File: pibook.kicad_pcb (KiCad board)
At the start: 2 copper layers, 85 x 85 mm, 161 parts, among them IC1 ATTINY48-A, J1 ComputeModule, J2 TRS_JACK_3PIN, P1 CONN_01X40, P2 USB_OTG, P3 CONN_01X02, P4 CONN_02X05, P5 USB_A, P6 CONN_02X06, P7 CONN_01X20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

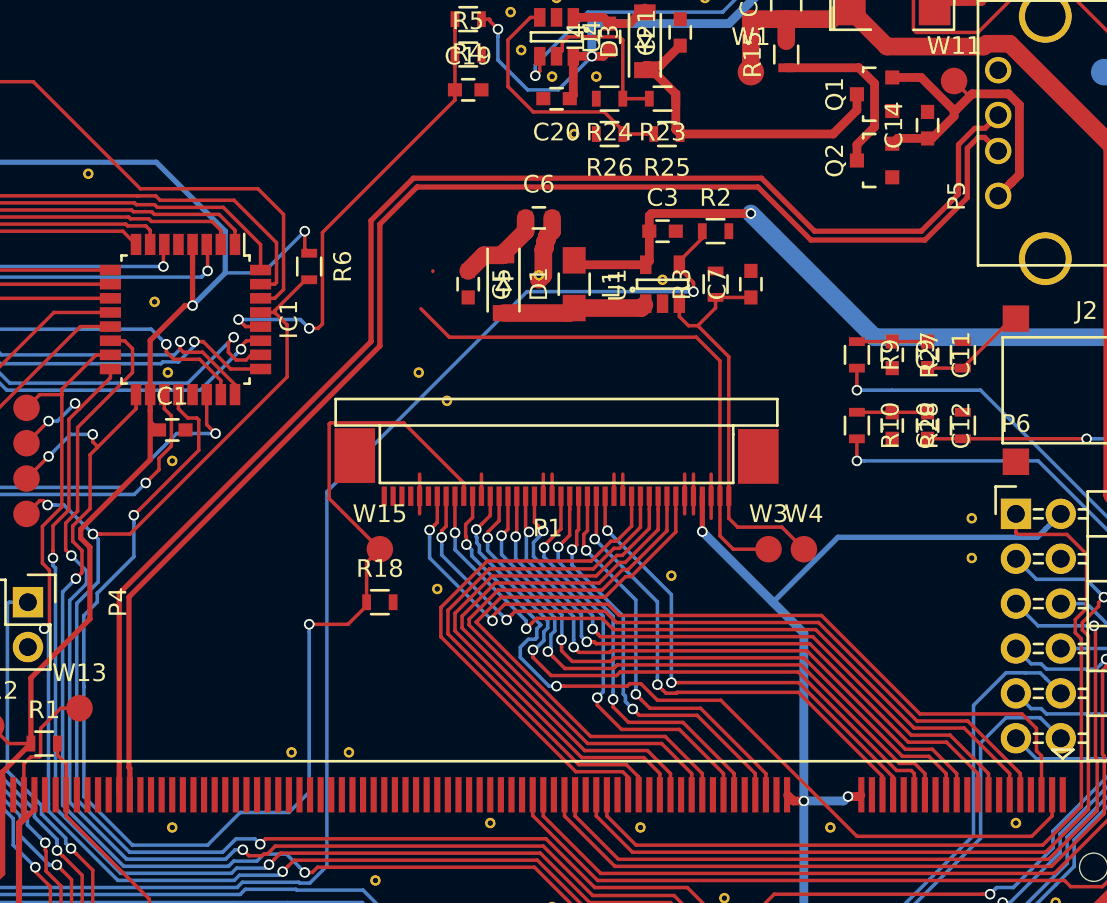
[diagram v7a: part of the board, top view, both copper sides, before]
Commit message: Improved USB impedance - 97 ohms diff vs 120
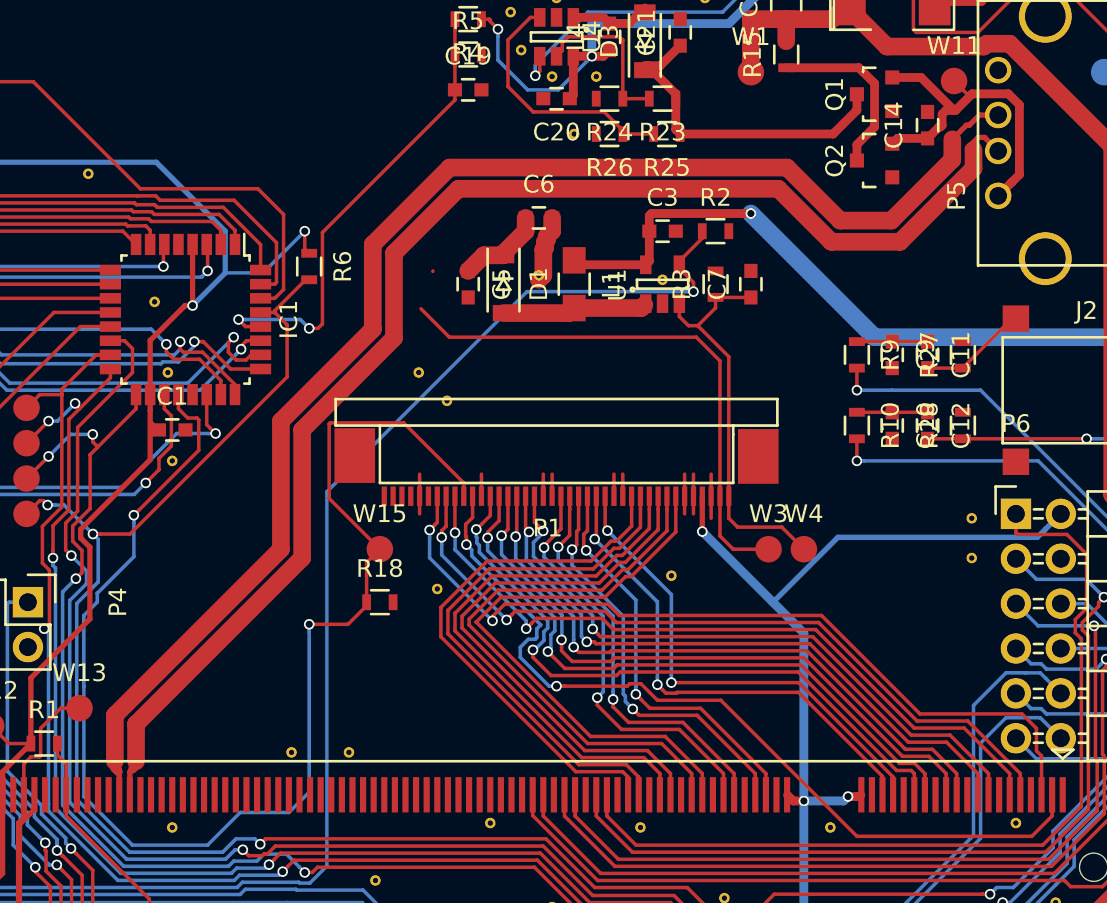
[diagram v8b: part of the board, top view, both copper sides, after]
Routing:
- net /USB_D+: track 79.7 -> 77.9 mm
- net /USB_D-: track 80.5 -> 79.4 mm
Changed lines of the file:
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@@
     (thickness 1.6)
     (drawings 25)
-    (tracks 1608)
+    (tracks 1627)
     (zones 0)
     (modules 161)
@@
   )
   (setup
-    (last_trace_width 0.2)
+    (last_trace_width 0.3)
     (user_trace_width 0.3)
     (user_trace_width 0.5)
@@
   (segment (start 144 140.75) (end 151 140.75) (width 0.2) (layer F.Cu) (net 10))
   (via (at 151 140.75) (size 0.6) (drill 0.4) (layers F.Cu B.Cu) (net 10))
+  (segment (start 143.5 122.164998) (end 143.035002 122.164998) (width 0.5) (layer F.Cu) (net 11))
+  (segment (start 143.035002 122.164998) (end 142.824001 122.375999) (width 0.5) (layer F.Cu) (net 11))
+  (segment (start 142.824001 122.375999) (end 142.824001 123.009201) (width 0.5) (layer F.Cu) (net 11))
+  (segment (start 142.824001 123.009201) (end 142.734201 123.099001) (width 0.5) (layer F.Cu) (net 11))
+  (segment (start 142.650999 123.099001) (end 142 123.75) (width 0.5) (layer F.Cu) (net 11))
+  (segment (start 142.734201 123.099001) (end 142.650999 123.099001) (width 0.5) (layer F.Cu) (net 11))
   (segment (start 143.5 120.5) (end 144.249999 121.249999) (width 0.2) (layer F.Cu) (net 11))
   (segment (start 144.249999 121.249999) (end 144.500001 121.249999) (width 0.2) (layer F.Cu) (net 11))
   (segment (start 144.500001 121.249999) (end 144.523431 121.226569) (width 0.2) (layer F.Cu) (net 11))
-  (segment (start 143.5 122.164998) (end 143.5 122.5) (width 0.5) (layer F.Cu) (net 11))
-  (segment (start 143.5 122.5) (end 142.25 123.75) (width 0.5) (layer F.Cu) (net 11))
-  (segment (start 142.25 123.75) (end 142 123.75) (width 0.5) (layer F.Cu) (net 11))
   (segment (start 143.585002 122.164998) (end 144.523431 121.226569) (width 0.5) (layer F.Cu) (net 11))
   (segment (start 144.523431 121.226569) (end 146.574155 121.226569) (width 0.5) (layer F.Cu) (net 11))
@@
   (segment (start 147 157.7) (end 148.163601 158.863601) (width 0.2) (layer B.Cu) (net 55))
   (via (at 152.903647 158.157519) (size 0.6) (drill 0.4) (layers F.Cu B.Cu) (net 55))
+  (segment (start 144.6 124.4) (end 144.6 125.448528) (width 1) (layer F.Cu) (net 56))
+  (segment (start 144.6 125.448528) (end 140.448528 129.6) (width 1) (layer F.Cu) (net 56))
+  (segment (start 106.6 140.248528) (end 106.6 147.498528) (width 1) (layer F.Cu) (net 56))
+  (segment (start 140.448528 129.6) (end 136.551472 129.6) (width 1) (layer F.Cu) (net 56))
+  (segment (start 97.2 156.898528) (end 97.2 159) (width 1) (layer F.Cu) (net 56))
+  (segment (start 136.551472 129.6) (end 133.551472 126.6) (width 1) (layer F.Cu) (net 56))
+  (segment (start 133.551472 126.6) (end 115.448528 126.6) (width 1) (layer F.Cu) (net 56))
+  (segment (start 115.448528 126.6) (end 111.8 130.248528) (width 1) (layer F.Cu) (net 56))
+  (segment (start 111.8 130.248528) (end 111.8 135.048528) (width 1) (layer F.Cu) (net 56))
+  (segment (start 111.8 135.048528) (end 106.6 140.248528) (width 1) (layer F.Cu) (net 56))
+  (segment (start 106.6 147.498528) (end 97.2 156.898528) (width 1) (layer F.Cu) (net 56))
+  (segment (start 144.25 124.310539) (end 144.510539 124.310539) (width 0.3) (layer F.Cu) (net 56))
+  (segment (start 144.510539 124.310539) (end 144.6 124.4) (width 0.3) (layer F.Cu) (net 56))
+  (segment (start 97.2 159) (end 97.2 159.25) (width 0.2) (layer F.Cu) (net 56))
+  (segment (start 96.85 159.6) (end 97 159.45) (width 0.3) (layer F.Cu) (net 56))
+  (segment (start 97 159.45) (end 97.2 159.25) (width 0.5) (layer F.Cu) (net 56))
+  (segment (start 96.85 160.9) (end 96.85 159.6) (width 0.3) (layer F.Cu) (net 56))
+  (segment (start 97.2 159.25) (end 97.2 159.2) (width 0.3) (layer F.Cu) (net 56))
   (segment (start 145.99788 124.45914) (end 145.231879 123.693139) (width 0.3) (layer F.Cu) (net 56))
-  (segment (start 113.103552 126.5) (end 111 128.603552) (width 0.3) (layer F.Cu) (net 56))
   (segment (start 145.231879 123.693139) (end 144.8674 123.693139) (width 0.3) (layer F.Cu) (net 56))
-  (segment (start 135.396448 129.5) (end 132.396448 126.5) (width 0.3) (layer F.Cu) (net 56))
   (segment (start 144.8674 123.693139) (end 144.25 124.310539) (width 0.3) (layer F.Cu) (net 56))
-  (segment (start 144.25 127.103552) (end 141.853552 129.5) (width 0.3) (layer F.Cu) (net 56))
-  (segment (start 132.396448 126.5) (end 113.103552 126.5) (width 0.3) (layer F.Cu) (net 56))
-  (segment (start 144.25 124.310539) (end 144.25 127.103552) (width 0.3) (layer F.Cu) (net 56))
-  (segment (start 141.853552 129.5) (end 135.396448 129.5) (width 0.3) (layer F.Cu) (net 56))
-  (segment (start 111 128.603552) (end 111 135.5) (width 0.3) (layer F.Cu) (net 56))
-  (segment (start 111 135.5) (end 96.8 149.7) (width 0.3) (layer F.Cu) (net 56))
-  (segment (start 96.8 149.7) (end 96.8 159.35) (width 0.3) (layer F.Cu) (net 56))
-  (segment (start 96.8 159.35) (end 96.85 159.4) (width 0.3) (layer F.Cu) (net 56))
-  (segment (start 96.85 159.4) (end 96.85 160.9) (width 0.3) (layer F.Cu) (net 56))
-  (segment (start 145.99788 122.42714) (end 145.247311 123.177709) (width 0.3) (layer F.Cu) (net 57))
-  (segment (start 145.247311 123.177709) (end 144.670834 123.177709) (width 0.3) (layer F.Cu) (net 57))
-  (segment (start 144.670834 123.177709) (end 143.749989 124.098554) (width 0.3) (layer F.Cu) (net 57))
-  (segment (start 143.749989 124.098554) (end 143.749989 126.896441) (width 0.3) (layer F.Cu) (net 57))
-  (segment (start 143.749989 126.896441) (end 141.646441 128.999989) (width 0.3) (layer F.Cu) (net 57))
-  (segment (start 141.646441 128.999989) (end 135.603541 128.999989) (width 0.3) (layer F.Cu) (net 57))
-  (segment (start 112.896448 126) (end 110.49999 128.396458) (width 0.3) (layer F.Cu) (net 57))
-  (segment (start 135.603541 128.999989) (end 132.603552 126) (width 0.3) (layer F.Cu) (net 57))
-  (segment (start 110.49999 128.396458) (end 110.49999 135.25001) (width 0.3) (layer F.Cu) (net 57))
-  (segment (start 132.603552 126) (end 112.896448 126) (width 0.3) (layer F.Cu) (net 57))
-  (segment (start 110.49999 135.25001) (end 96.25 149.5) (width 0.3) (layer F.Cu) (net 57))
-  (segment (start 96.25 149.5) (end 96.25 160.9) (width 0.3) (layer F.Cu) (net 57))
+  (segment (start 144.2 123) (end 143.4 123.8) (width 0.3) (layer F.Cu) (net 57))
+  (segment (start 96 159) (end 96 156.401472) (width 1) (layer F.Cu) (net 57))
+  (segment (start 105.4 147.001472) (end 105.4 139.751472) (width 1) (layer F.Cu) (net 57))
+  (segment (start 143.4 124.951472) (end 143.4 123.8) (width 1) (layer F.Cu) (net 57))
+  (segment (start 96 156.401472) (end 105.4 147.001472) (width 1) (layer F.Cu) (net 57))
+  (segment (start 105.4 139.751472) (end 110.6 134.551472) (width 1) (layer F.Cu) (net 57))
+  (segment (start 110.6 134.551472) (end 110.6 129.751472) (width 1) (layer F.Cu) (net 57))
+  (segment (start 110.6 129.751472) (end 114.951472 125.4) (width 1) (layer F.Cu) (net 57))
+  (segment (start 114.951472 125.4) (end 134.048528 125.4) (width 1) (layer F.Cu) (net 57))
+  (segment (start 134.048528 125.4) (end 137.048528 128.4) (width 1) (layer F.Cu) (net 57))
+  (segment (start 137.048528 128.4) (end 139.951472 128.4) (width 1) (layer F.Cu) (net 57))
+  (segment (start 139.951472 128.4) (end 143.4 124.951472) (width 1) (layer F.Cu) (net 57))
+  (segment (start 145.99788 122.42714) (end 144.936414 122.42714) (width 0.3) (layer F.Cu) (net 57))
+  (segment (start 144.936414 122.42714) (end 144.363554 123) (width 0.3) (layer F.Cu) (net 57))
+  (segment (start 144.363554 123) (end 144.2 123) (width 0.3) (layer F.Cu) (net 57))
+  (segment (start 96.25 159.45) (end 96.05 159.45) (width 0.2) (layer F.Cu) (net 57))
+  (segment (start 96.05 159.45) (end 96 159.4) (width 0.2) (layer F.Cu) (net 57))
+  (segment (start 96.25 160.9) (end 96.25 159.45) (width 0.3) (layer F.Cu) (net 57))
+  (segment (start 96.2 159.6) (end 96 159.4) (width 0.5) (layer F.Cu) (net 57))
+  (segment (start 96 159.4) (end 96 159) (width 0.5) (layer F.Cu) (net 57))
+  (segment (start 96.25 159.45) (end 96.2 159.4) (width 0.3) (layer F.Cu) (net 57))
   (segment (start 98.254952 167.901897) (end 100.5 167.901897) (width 0.2) (layer B.Cu) (net 58))
   (segment (start 100.5 167.901897) (end 100.522623 167.901897) (width 0.2) (layer B.Cu) (net 58))
